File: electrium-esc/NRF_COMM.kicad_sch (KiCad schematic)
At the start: 0 parts

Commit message: Add additional connections to MCU
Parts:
- added C?: 47u, symbol Device:C
- added U?: NRF24L01_Breakout, RF_Module:nRF24L01_Breakout, symbol RF:NRF24L01_Breakout
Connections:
- new net +3.3V: C?.1, U?.2 (VCC)
- new net GND: C?.2, U?.1 (GND)
- new net NRF_CE: U?.3 (CE)
- new net NRF_CSN: U?.4 (~{CSN})
- new net NRF_MISO: U?.7 (MISO)
- new net NRF_MOSI: U?.6 (MOSI)
- new net NRF_SCK: U?.5 (SCK)
- no-connect marks 0 -> 1
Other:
- company: (none) -> Electrium Mobility
- title: (none) -> BLDC Electronic Speed Controller 1.0
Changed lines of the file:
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@@
 (kicad_sch (version 20211123) (generator eeschema)
   (paper "A4")
+  (title_block
+    (title "BLDC Electronic Speed Controller 1.0")
+    (date "2023-01-19")
+    (rev "ESC 1.0")
+    (company "Electrium Mobility")
+    (comment 1 "NRF Chip")
+  )
+  (junction (at 154.94 66.04) (diameter 0) (color 0 0 0 0)
+  )
+  (no_connect (at 142.24 102.87))
+  (wire (pts (xy 161.29 66.04) (xy 161.29 67.31))
+    (stroke (width 0) (type default) (color 0 0 0 0))
+  )
+  (wire (pts (xy 154.94 66.04) (xy 161.29 66.04))
+    (stroke (width 0) (type default) (color 0 0 0 0))
+  )
+  (wire (pts (xy 154.94 66.04) (xy 154.94 80.01))
+    (stroke (width 0) (type default) (color 0 0 0 0))
+  )
+  (wire (pts (xy 154.94 64.77) (xy 154.94 66.04))
+    (stroke (width 0) (type default) (color 0 0 0 0))
+  )
+  (hierarchical_label "NRF_SCK" (shape input) (at 142.24 92.71 180)
+    (effects (font (size 1.27 1.27)) (justify right))
+  )
+  (hierarchical_label "NRF_MISO" (shape output) (at 142.24 90.17 180)
+    (effects (font (size 1.27 1.27)) (justify right))
+  )
+  (hierarchical_label "NRF_MOSI" (shape input) (at 142.24 87.63 180)
+    (effects (font (size 1.27 1.27)) (justify right))
+  )
+  (hierarchical_label "NRF_CE" (shape input) (at 142.24 100.33 180)
+    (effects (font (size 1.27 1.27)) (justify right))
+  )
+  (hierarchical_label "NRF_CSN" (shape input) (at 142.24 95.25 180)
+    (effects (font (size 1.27 1.27)) (justify right))
+  )
+  (symbol (lib_id "power:GND") (at 154.94 110.49 0) (unit 1)
+    (in_bom yes) (on_board yes)
+    (property "Reference" "#PWR?" (id 0) (at 154.94 116.84 0)
+      (effects (font (size 1.27 1.27)) hide)
+    )
+    (property "Value" "GND" (id 1) (at 154.94 114.3 0))
+    (property "Footprint" "" (id 2) (at 154.94 110.49 0)
+      (effects (font (size 1.27 1.27)) hide)
+    )
+    (property "Datasheet" "" (id 3) (at 154.94 110.49 0)
+      (effects (font (size 1.27 1.27)) hide)
+    )
+    (pin "1")
+  )
+  (symbol (lib_id "power:GND") (at 161.29 74.93 0) (unit 1)
+    (in_bom yes) (on_board yes)
+    (property "Reference" "#PWR?" (id 0) (at 161.29 81.28 0)
+      (effects (font (size 1.27 1.27)) hide)
+    )
+    (property "Value" "GND" (id 1) (at 161.29 78.74 0))
+    (property "Footprint" "" (id 2) (at 161.29 74.93 0)
+      (effects (font (size 1.27 1.27)) hide)
+    )
+    (property "Datasheet" "" (id 3) (at 161.29 74.93 0)
+      (effects (font (size 1.27 1.27)) hide)
+    )
+    (pin "1")
+  )
+  (symbol (lib_id "Device:C") (at 161.29 71.12 0) (unit 1)
+    (in_bom yes) (on_board yes) (fields_autoplaced)
+    (property "Reference" "C?" (id 0) (at 165.1 69.8499 0)
+      (effects (font (size 1.27 1.27)) (justify left))
+    )
+    (property "Value" "47u" (id 1) (at 165.1 72.3899 0)
+      (effects (font (size 1.27 1.27)) (justify left))
+    )
+    (property "Footprint" "" (id 2) (at 162.2552 74.93 0)
+      (effects (font (size 1.27 1.27)) hide)
+    )
+    (property "Datasheet" "~" (id 3) (at 161.29 71.12 0)
+      (effects (font (size 1.27 1.27)) hide)
+    )
+    (pin "1")
+    (pin "2")
+  )
+  (symbol (lib_id "RF:NRF24L01_Breakout") (at 154.94 95.25 0) (unit 1)
+    (in_bom yes) (on_board yes)
+    (property "Reference" "U?" (id 0) (at 160.02 82.55 0)
+      (effects (font (size 1.27 1.27)) (justify left))
+    )
+    (property "Value" "NRF24L01_Breakout" (id 1) (at 160.02 109.22 0)
+      (effects (font (size 1.27 1.27)) (justify left))
+    )
+    (property "Footprint" "RF_Module:nRF24L01_Breakout" (id 2) (at 158.75 80.01 0)
+      (effects (font (size 1.27 1.27) italic) (justify left) hide)
+    )
+    (property "Datasheet" "http://www.nordicsemi.com/eng/content/download/2730/34105/file/nRF24L01_Product_Specification_v2_0.pdf" (id 3) (at 154.94 97.79 0)
+      (effects (font (size 1.27 1.27)) hide)
+    )
+    (pin "1")
+    (pin "2")
+    (pin "3")
+    (pin "4")
+    (pin "5")
+    (pin "6")
+    (pin "7")
+    (pin "8")
+  )
+  (symbol (lib_id "power:+3.3V") (at 154.94 64.77 0) (unit 1)
+    (in_bom yes) (on_board yes) (fields_autoplaced)
+    (property "Reference" "#PWR?" (id 0) (at 154.94 68.58 0)
+      (effects (font (size 1.27 1.27)) hide)
+    )
+    (property "Value" "+3.3V" (id 1) (at 154.94 59.69 0))
+    (property "Footprint" "" (id 2) (at 154.94 64.77 0)
+      (effects (font (size 1.27 1.27)) hide)
+    )
+    (property "Datasheet" "" (id 3) (at 154.94 64.77 0)
+      (effects (font (size 1.27 1.27)) hide)
+    )
+    (pin "1")
+  )
 )

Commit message: Fix Error
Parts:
- C77: renamed from C?; footprint (none) -> Capacitor_THT:CP_Radial_D10.0mm_P5.00mm
- gave numbers to parts that had none: 1
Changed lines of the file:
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@@
   (symbol (lib_id "power:GND") (at 154.94 110.49 0) (unit 1)
     (in_bom yes) (on_board yes)
-    (property "Reference" "#PWR?" (id 0) (at 154.94 116.84 0)
+    (property "Reference" "#PWR0171" (id 0) (at 154.94 116.84 0)
       (effects (font (size 1.27 1.27)) hide)
     )
@@
   (symbol (lib_id "power:GND") (at 161.29 74.93 0) (unit 1)
     (in_bom yes) (on_board yes)
-    (property "Reference" "#PWR?" (id 0) (at 161.29 81.28 0)
+    (property "Reference" "#PWR0172" (id 0) (at 161.29 81.28 0)
       (effects (font (size 1.27 1.27)) hide)
     )
@@
   (symbol (lib_id "Device:C") (at 161.29 71.12 0) (unit 1)
     (in_bom yes) (on_board yes) (fields_autoplaced)
-    (property "Reference" "C?" (id 0) (at 165.1 69.8499 0)
+    (property "Reference" "C77" (id 0) (at 165.1 69.8499 0)
       (effects (font (size 1.27 1.27)) (justify left))
     )
@@
       (effects (font (size 1.27 1.27)) (justify left))
     )
-    (property "Footprint" "" (id 2) (at 162.2552 74.93 0)
+    (property "Footprint" "Capacitor_THT:CP_Radial_D10.0mm_P5.00mm" (id 2) (at 162.2552 74.93 0)
       (effects (font (size 1.27 1.27)) hide)
     )
@@
   (symbol (lib_id "RF:NRF24L01_Breakout") (at 154.94 95.25 0) (unit 1)
     (in_bom yes) (on_board yes)
-    (property "Reference" "U?" (id 0) (at 160.02 82.55 0)
+    (property "Reference" "U5" (id 0) (at 160.02 82.55 0)
       (effects (font (size 1.27 1.27)) (justify left))
     )
@@
   (symbol (lib_id "power:+3.3V") (at 154.94 64.77 0) (unit 1)
     (in_bom yes) (on_board yes) (fields_autoplaced)
-    (property "Reference" "#PWR?" (id 0) (at 154.94 68.58 0)
+    (property "Reference" "#PWR0173" (id 0) (at 154.94 68.58 0)
       (effects (font (size 1.27 1.27)) hide)
     )

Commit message: Update footprints
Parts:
- C77: footprint Capacitor_THT:CP_Radial_D10.0mm_P5.00mm -> Capacitor_THT:CP_Radial_D4.0mm_P1.50mm
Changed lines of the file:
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@@
       (effects (font (size 1.27 1.27)) (justify left))
     )
-    (property "Footprint" "Capacitor_THT:CP_Radial_D10.0mm_P5.00mm" (id 2) (at 162.2552 74.93 0)
+    (property "Footprint" "Capacitor_THT:CP_Radial_D4.0mm_P1.50mm" (id 2) (at 162.2552 74.93 0)
       (effects (font (size 1.27 1.27)) hide)
     )

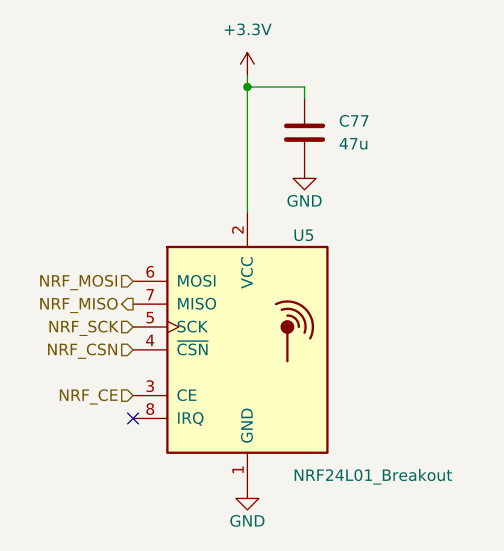
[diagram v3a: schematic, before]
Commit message: relabel components to make more sense
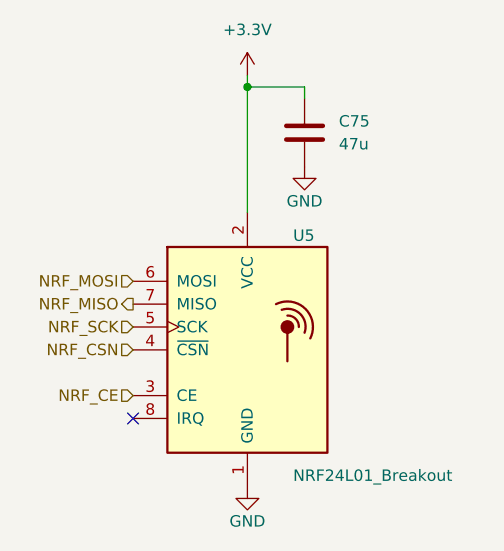
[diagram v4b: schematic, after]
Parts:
- renumbered C77 to C75
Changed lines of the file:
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@@
   (symbol (lib_id "power:GND") (at 154.94 110.49 0) (unit 1)
     (in_bom yes) (on_board yes)
-    (property "Reference" "#PWR0171" (id 0) (at 154.94 116.84 0)
+    (property "Reference" "#PWR073" (id 0) (at 154.94 116.84 0)
       (effects (font (size 1.27 1.27)) hide)
     )
@@
   (symbol (lib_id "power:GND") (at 161.29 74.93 0) (unit 1)
     (in_bom yes) (on_board yes)
-    (property "Reference" "#PWR0172" (id 0) (at 161.29 81.28 0)
+    (property "Reference" "#PWR072" (id 0) (at 161.29 81.28 0)
       (effects (font (size 1.27 1.27)) hide)
     )
@@
   (symbol (lib_id "Device:C") (at 161.29 71.12 0) (unit 1)
     (in_bom yes) (on_board yes) (fields_autoplaced)
-    (property "Reference" "C77" (id 0) (at 165.1 69.8499 0)
+    (property "Reference" "C75" (id 0) (at 165.1 69.8499 0)
       (effects (font (size 1.27 1.27)) (justify left))
     )
@@
   (symbol (lib_id "power:+3.3V") (at 154.94 64.77 0) (unit 1)
     (in_bom yes) (on_board yes) (fields_autoplaced)
-    (property "Reference" "#PWR0173" (id 0) (at 154.94 68.58 0)
+    (property "Reference" "#PWR071" (id 0) (at 154.94 68.58 0)
       (effects (font (size 1.27 1.27)) hide)
     )
